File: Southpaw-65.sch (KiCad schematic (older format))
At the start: 196 parts, among them J1 USB_C_Receptacle_USB2.0, SW1 SW_Push, U1 ATmega32A-PU, Y1 16MHz

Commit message: Added capacitators and created top row in pcbnew
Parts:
- C1, C3, C4, C5, C6, C7: footprint (none) -> Capacitor_THT:CP_Radial_Tantal_D5.0mm_P2.50mm
- C8: footprint (none) -> Capacitor_THT:CP_Radial_D18.0mm_P7.50mm
- MX4-10: footprint MX_Alps_Hybrid:MX-1U -> MX_Alps_Hybrid:MX-7U
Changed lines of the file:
@@
 F 0 "C7" H 3592 7346 50  0000 L CNN
 F 1 "10uF" H 3592 7255 50  0000 L CNN
-F 2 "" H 3500 7300 50  0001 C CNN
+F 2 "Capacitor_THT:CP_Radial_Tantal_D5.0mm_P2.50mm" H 3500 7300 50  0001 C CNN
 F 3 "~" H 3500 7300 50  0001 C CNN
 	1    3500 7300
@@
 F 0 "C6" H 3092 7346 50  0000 L CNN
 F 1 "100nF" H 3092 7255 50  0000 L CNN
-F 2 "" H 3000 7300 50  0001 C CNN
+F 2 "Capacitor_THT:CP_Radial_Tantal_D5.0mm_P2.50mm" H 3000 7300 50  0001 C CNN
 F 3 "~" H 3000 7300 50  0001 C CNN
 	1    3000 7300
@@
 F 0 "C5" H 2592 7346 50  0000 L CNN
 F 1 "100nF" H 2592 7255 50  0000 L CNN
-F 2 "" H 2500 7300 50  0001 C CNN
+F 2 "Capacitor_THT:CP_Radial_Tantal_D5.0mm_P2.50mm" H 2500 7300 50  0001 C CNN
 F 3 "~" H 2500 7300 50  0001 C CNN
 	1    2500 7300
@@
 F 0 "C4" H 2092 7346 50  0000 L CNN
 F 1 "100nF" H 2092 7255 50  0000 L CNN
-F 2 "" H 2000 7300 50  0001 C CNN
+F 2 "Capacitor_THT:CP_Radial_Tantal_D5.0mm_P2.50mm" H 2000 7300 50  0001 C CNN
 F 3 "~" H 2000 7300 50  0001 C CNN
 	1    2000 7300
@@
 F 0 "C3" V 4721 6950 50  0000 C CNN
 F 1 "22pF" V 4812 6950 50  0000 C CNN
-F 2 "" H 4950 6950 50  0001 C CNN
+F 2 "Capacitor_THT:CP_Radial_Tantal_D5.0mm_P2.50mm" H 4950 6950 50  0001 C CNN
 F 3 "~" H 4950 6950 50  0001 C CNN
 	1    4950 6950
@@
 F 0 "C1" V 4721 6450 50  0000 C CNN
 F 1 "22pF" V 4812 6450 50  0000 C CNN
-F 2 "" H 4950 6450 50  0001 C CNN
+F 2 "Capacitor_THT:CP_Radial_Tantal_D5.0mm_P2.50mm" H 4950 6450 50  0001 C CNN
 F 3 "~" H 4950 6450 50  0001 C CNN
 	1    4950 6450
@@
 F 0 "C8" H 4042 7346 50  0000 L CNN
 F 1 "1uF" H 4042 7255 50  0000 L CNN
-F 2 "" H 3950 7300 50  0001 C CNN
+F 2 "Capacitor_THT:CP_Radial_D18.0mm_P7.50mm" H 3950 7300 50  0001 C CNN
 F 3 "~" H 3950 7300 50  0001 C CNN
 	1    3950 7300
@@
 F 0 "MX4-10" H 11883 4273 60  0000 C CNN
 F 1 "MX-NoLED" H 11883 4199 20  0000 C CNN
-F 2 "MX_Alps_Hybrid:MX-1U" H 11225 4025 60  0001 C CNN
+F 2 "MX_Alps_Hybrid:MX-7U" H 11225 4025 60  0001 C CNN
 F 3 "" H 11225 4025 60  0001 C CNN
 	1    11850 4050
@@
 	17200 4200 17050 4200
 $Comp
-L MX_Alps_Hybrid:MX-NoLED MX4-8
-U 1 1 5FBEA516
-P 10650 4050
-F 0 "MX4-8" H 10683 4273 60  0000 C CNN
-F 1 "MX-NoLED" H 10683 4199 20  0000 C CNN
-F 2 "MX_Alps_Hybrid:MX-3U" H 10025 4025 60  0001 C CNN
-F 3 "" H 10025 4025 60  0001 C CNN
-	1    10650 4050
-	1    0    0    -1
-$EndComp
-$Comp
 L Device:D_Small D4-8
 U 1 1 5FBEA520
@@
 Connection ~ 8000 3100
 Connection ~ 6700 3100
+$Comp
+L MX_Alps_Hybrid:MX-NoLED MX4-8
+U 1 1 5FBEA516
+P 10650 4050
+F 0 "MX4-8" H 10683 4273 60  0000 C CNN
+F 1 "MX-NoLED" H 10683 4199 20  0000 C CNN
+F 2 "MX_Alps_Hybrid:MX-3U" H 10025 4025 60  0001 C CNN
+F 3 "" H 10025 4025 60  0001 C CNN
+	1    10650 4050
+	1    0    0    -1
+$EndComp
 $EndSCHEMATC

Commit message: Backup #3
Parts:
- removed Y1: 16MHz, Crystal:Crystal_HC49-U_Vertical, symbol Device:Crystal_GND24_Small
- added Y1: 16MHz, Crystal:Crystal_HC49-U_Horizontal, symbol Device:Crystal
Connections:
- wire segments 314 -> 313
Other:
- moved on the sheet: C1, C3, D1-11, D1-15, D2-11, D2-15, D3-11, D3-15, D4-15, MX1-11, MX1-15, MX2-11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

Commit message: Started tracing and working on pathing
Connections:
- net COL0: now also MX1-0.1 (COL), MX2-0.1 (COL), MX3-0.1 (COL), MX4-0.1 (COL)
- net REA: now reaches U1.18 (PD4)
- net REB: now reaches U1.19 (PD5)
- net at D0-7.2 (A): now also MX0-7.2 (ROW)
- no-connect marks 5 -> 3
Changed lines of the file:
@@
 	1    0    0    -1
 $EndComp
-Text Notes 5250 5000 0    50   ~ 0
-Reset
 Text Notes 5200 6100 0    50   ~ 0
 Crystal
@@
 	0    -1   -1   0
 $EndComp
-Wire Wire Line
-	10000 1600 9850 1600
 $Comp
 L MX_Alps_Hybrid:MX-NoLED MX0-8
@@
 NoConn ~ 2000 4450
 NoConn ~ 2000 4350
-NoConn ~ 2000 4250
-NoConn ~ 2000 4150
 NoConn ~ 2000 3850
 Wire Wire Line
@@
 	5300 6800 5300 6850
 Connection ~ 5300 6800
+Wire Wire Line
+	5250 2050 5250 1400
+Connection ~ 5250 2050
+Connection ~ 5250 1400
+Wire Wire Line
+	9800 1600 10000 1600
+Text Notes 5250 5000 0    50   ~ 0
+Reset
+Text GLabel 2000 4150 2    50   Input ~ 0
+REA
+Text GLabel 2000 4250 2    50   Input ~ 0
+REB
 $EndSCHEMATC

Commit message: Finished all tracks
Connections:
- net COL18: now also MX1-18.1 (COL), MX2-18.1 (COL), MX3-18.1 (COL), MX4-18.1 (COL)
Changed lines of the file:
@@
 	14150 2250 14000 2250
-$Comp
-L MX_Alps_Hybrid:MX-NoLED MX1-18
-U 1 1 5FAA0BCC
-P 16650 2100
-F 0 "MX1-18" H 16683 2323 60  0000 C CNN
-F 1 "MX-NoLED" H 16683 2249 20  0000 C CNN
-F 2 "MX_Alps_Hybrid:MX-1.5U" H 16025 2075 60  0001 C CNN
-F 3 "" H 16025 2075 60  0001 C CNN
-	1    16650 2100
-	1    0    0    -1
-$EndComp
 $Comp
 L Device:D_Small D1-18
@@
 Wire Wire Line
 	17400 1400 17400 2050
-Wire Wire Line
-	16800 2050 16800 2700
 Connection ~ 16800 2700
 Wire Wire Line
@@
 Text GLabel 2000 4250 2    50   Input ~ 0
 REB
+Wire Wire Line
+	16800 2050 16800 2700
+$Comp
+L MX_Alps_Hybrid:MX-NoLED MX1-18
+U 1 1 5FAA0BCC
+P 16650 2100
+F 0 "MX1-18" H 16683 2323 60  0000 C CNN
+F 1 "MX-NoLED" H 16683 2249 20  0000 C CNN
+F 2 "MX_Alps_Hybrid:MX-1.5U" H 16025 2075 60  0001 C CNN
+F 3 "" H 16025 2075 60  0001 C CNN
+	1    16650 2100
+	1    0    0    -1
+$EndComp
+Wire Wire Line
+	16800 1400 16800 2050
+Connection ~ 16800 1400
+Connection ~ 16800 2050
 $EndSCHEMATC

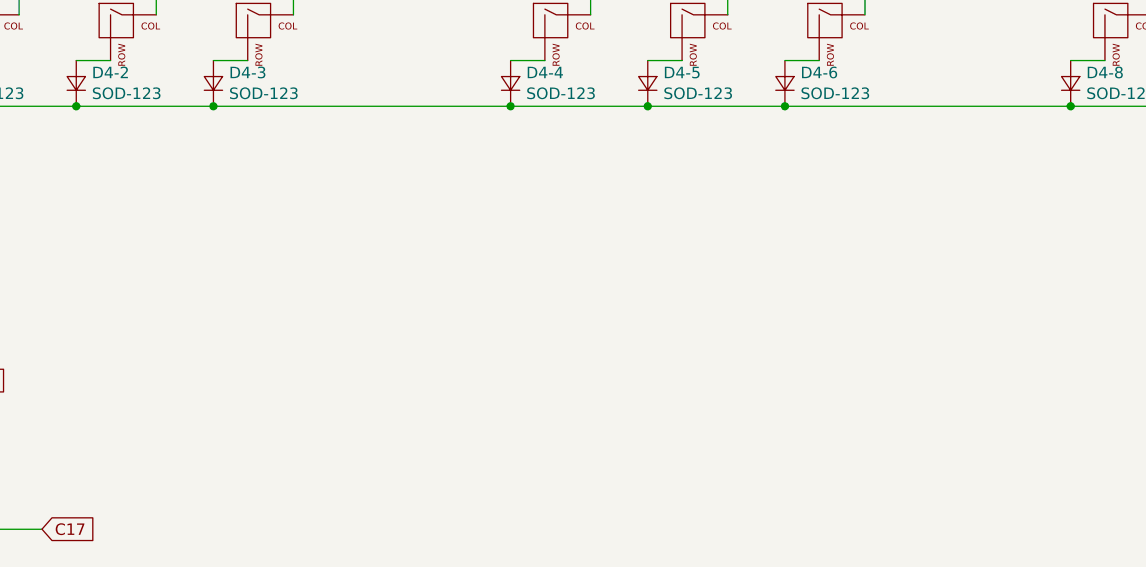
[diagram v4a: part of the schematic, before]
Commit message: Added mounting holes to pcb added changed dimensions of PCB
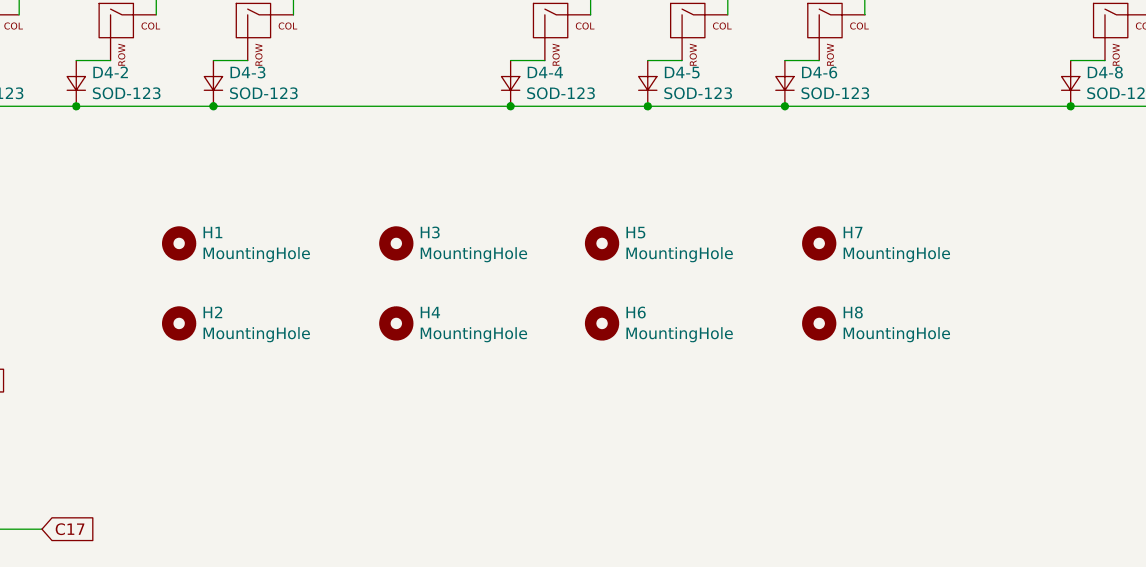
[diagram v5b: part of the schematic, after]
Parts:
- added H1, H2, H3, H4, H5, H6, H7, H8: MountingHole, MountingHole:MountingHole_3.2mm_M3, symbol Mechanical:MountingHole
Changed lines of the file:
@@
 Connection ~ 16800 1400
 Connection ~ 16800 2050
+$Comp
+L Mechanical:MountingHole H1
+U 1 1 5F9978E5
+P 6550 5000
+F 0 "H1" H 6650 5046 50  0000 L CNN
+F 1 "MountingHole" H 6650 4955 50  0000 L CNN
+F 2 "MountingHole:MountingHole_3.2mm_M3" H 6550 5000 50  0001 C CNN
+F 3 "~" H 6550 5000 50  0001 C CNN
+	1    6550 5000
+	1    0    0    -1
+$EndComp
+$Comp
+L Mechanical:MountingHole H2
+U 1 1 5F999F3C
+P 6550 5350
+F 0 "H2" H 6650 5396 50  0000 L CNN
+F 1 "MountingHole" H 6650 5305 50  0000 L CNN
+F 2 "MountingHole:MountingHole_3.2mm_M3" H 6550 5350 50  0001 C CNN
+F 3 "~" H 6550 5350 50  0001 C CNN
+	1    6550 5350
+	1    0    0    -1
+$EndComp
+$Comp
+L Mechanical:MountingHole H3
+U 1 1 5F9B455A
+P 7500 5000
+F 0 "H3" H 7600 5046 50  0000 L CNN
+F 1 "MountingHole" H 7600 4955 50  0000 L CNN
+F 2 "MountingHole:MountingHole_3.2mm_M3" H 7500 5000 50  0001 C CNN
+F 3 "~" H 7500 5000 50  0001 C CNN
+	1    7500 5000
+	1    0    0    -1
+$EndComp
+$Comp
+L Mechanical:MountingHole H4
+U 1 1 5F9B4564
+P 7500 5350
+F 0 "H4" H 7600 5396 50  0000 L CNN
+F 1 "MountingHole" H 7600 5305 50  0000 L CNN
+F 2 "MountingHole:MountingHole_3.2mm_M3" H 7500 5350 50  0001 C CNN
+F 3 "~" H 7500 5350 50  0001 C CNN
+	1    7500 5350
+	1    0    0    -1
+$EndComp
+$Comp
+L Mechanical:MountingHole H5
+U 1 1 5F9CEEB3
+P 8400 5000
+F 0 "H5" H 8500 5046 50  0000 L CNN
+F 1 "MountingHole" H 8500 4955 50  0000 L CNN
+F 2 "MountingHole:MountingHole_3.2mm_M3" H 8400 5000 50  0001 C CNN
+F 3 "~" H 8400 5000 50  0001 C CNN
+	1    8400 5000
+	1    0    0    -1
+$EndComp
+$Comp
+L Mechanical:MountingHole H6
+U 1 1 5F9CEEBD
+P 8400 5350
+F 0 "H6" H 8500 5396 50  0000 L CNN
+F 1 "MountingHole" H 8500 5305 50  0000 L CNN
+F 2 "MountingHole:MountingHole_3.2mm_M3" H 8400 5350 50  0001 C CNN
+F 3 "~" H 8400 5350 50  0001 C CNN
+	1    8400 5350
+	1    0    0    -1
+$EndComp
+$Comp
+L Mechanical:MountingHole H7
+U 1 1 5F9CEEC7
+P 9350 5000
+F 0 "H7" H 9450 5046 50  0000 L CNN
+F 1 "MountingHole" H 9450 4955 50  0000 L CNN
+F 2 "MountingHole:MountingHole_3.2mm_M3" H 9350 5000 50  0001 C CNN
+F 3 "~" H 9350 5000 50  0001 C CNN
+	1    9350 5000
+	1    0    0    -1
+$EndComp
+$Comp
+L Mechanical:MountingHole H8
+U 1 1 5F9CEED1
+P 9350 5350
+F 0 "H8" H 9450 5396 50  0000 L CNN
+F 1 "MountingHole" H 9450 5305 50  0000 L CNN
+F 2 "MountingHole:MountingHole_3.2mm_M3" H 9350 5350 50  0001 C CNN
+F 3 "~" H 9350 5350 50  0001 C CNN
+	1    9350 5350
+	1    0    0    -1
+$EndComp
 $EndSCHEMATC
